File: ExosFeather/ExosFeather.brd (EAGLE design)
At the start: 50.8 x 22.9 mm, 12 parts, among them J2 TC_2050_IDC_TOP, J6 CONN_2X1_JST_PA, U1 MCP73831, U2 STM32L052KX

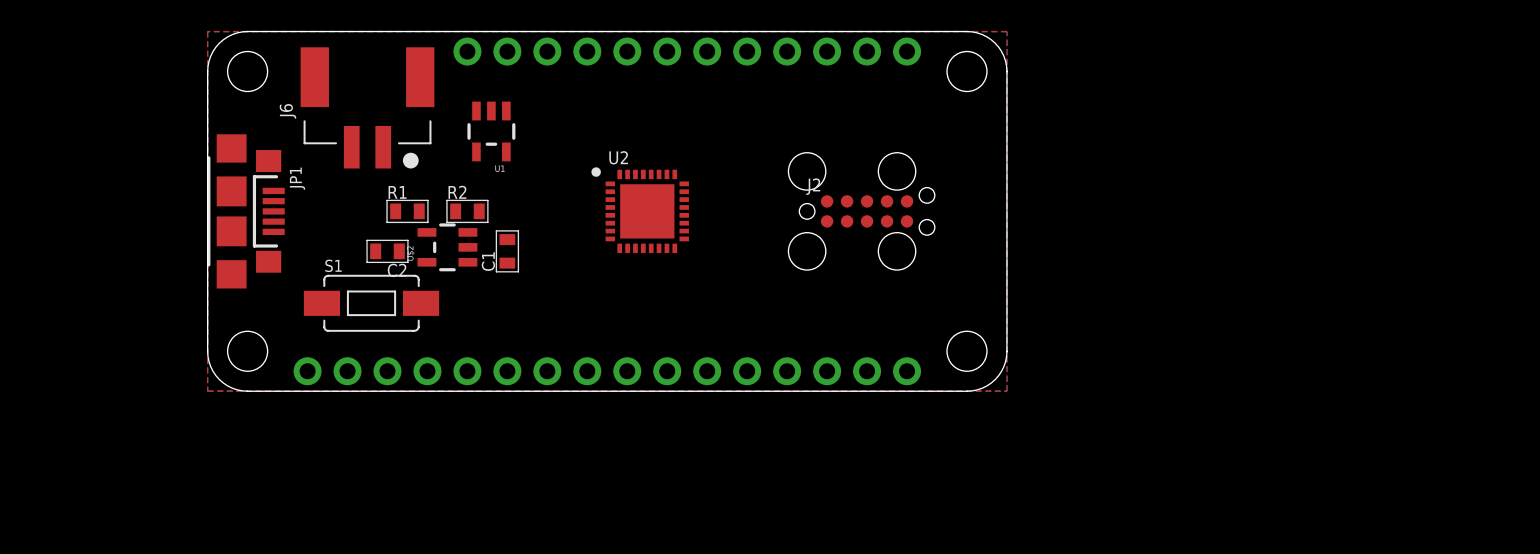
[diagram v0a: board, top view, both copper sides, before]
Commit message: exosfeather
updated the pinouts
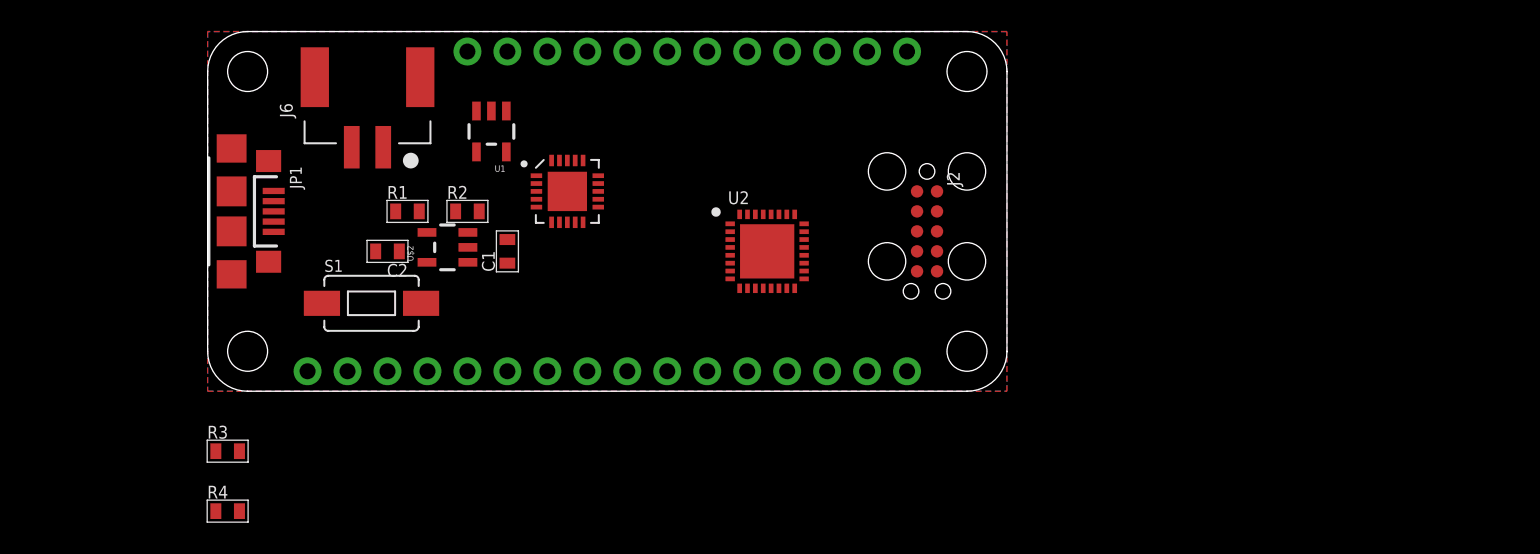
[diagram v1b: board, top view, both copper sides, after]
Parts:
- added R3, R4: (no value), stepOSP:0603
- added U$3: MCP73871, stepOSP:QFN_20_4X4
- moved U2 8.03 mm to (35.6, 8.89)
- moved J2 4.02 mm to (45.7, 10.2), turned to 270 degrees
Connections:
- new net CLK_IN: U$1.P$4, U2.6
- new net DAC: U$1.P$8, U2.10
- new net DE2: U$1.P$5, U2.7
- new net EVENT: U$1.P$23, U2.14
- new net MCO: U$1.P$24, U2.18
- new net MISO: U$1.P$16, U2.12
- new net MOSI: U$1.P$17, U2.13
- new net NRST: U$1.P$28, U2.4
- new net NSS: U$1.P$19, U2.25
- new net PB1: U$1.P$22, U2.15
- new net PB2: U$1.P$21, U2.16
- new net PB3: U$1.P$20, U2.26
- new net RX1: U$1.P$15, U2.20
- new net RX2: U$1.P$7, U2.9
- new net SCK: U$1.P$18, U2.11
- new net SCL: R3.P$1, U$1.P$11, U2.29
- new net SDA: R4.P$1, U$1.P$12, U2.30
- new net TIM22_CH1: U$1.P$9, U2.27
- new net TIM22_CH2: U$1.P$10, U2.28
- new net TX1: U$1.P$14, U2.19
- new net TX2: U$1.P$6, U2.8
- net +3V3: now also R3.P$2, R4.P$2
- net D+: now also U2.22
- net D-: now also U2.21
- net SW_CLK: now also U2.24
- net SW_DIO: now also U2.23
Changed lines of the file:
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@@
 <?xml version="1.0" encoding="utf-8"?>
 <!DOCTYPE eagle SYSTEM "eagle.dtd">
-<eagle version="7.7.0">
+<eagle version="7.3.0">
 <drawing>
 <settings>
@@
 <element name="R2" library="stepOSP" package="0603" value="" x="16.51" y="11.43"/>
 <element name="R1" library="stepOSP" package="0603" value="" x="12.7" y="11.43"/>
-<element name="U2" library="leaf" package="STM32_QFN_32_5X5" value="STM32L052KX" x="27.94" y="11.43"/>
-<element name="J2" library="leaf" package="TC_2050_IC_TOP" value="TC_2050_IDC_TOP" x="41.91" y="11.43"/>
+<element name="U2" library="leaf" package="STM32_QFN_32_5X5" value="STM32L052KX" x="35.56" y="8.89"/>
+<element name="J2" library="leaf" package="TC_2050_IC_TOP" value="TC_2050_IDC_TOP" x="45.72" y="10.16" rot="R270"/>
+<element name="R3" library="stepOSP" package="0603" value="" x="1.27" y="-3.81"/>
+<element name="R4" library="stepOSP" package="0603" value="" x="1.27" y="-7.62"/>
+<element name="U$3" library="stepOSP" package="QFN_20_4X4" value="MCP73871" x="22.86" y="12.7"/>
 </elements>
 <signals>
@@
 <contactref element="J2" pad="3"/>
 <contactref element="J2" pad="5"/>
-<wire x1="41.91" y1="10.795" x2="44.45" y2="10.795" width="0" layer="19" extent="1-1"/>
-<wire x1="44.45" y1="1.27" x2="44.45" y2="10.795" width="0" layer="19" extent="1-1"/>
-<wire x1="27.94" y1="11.43" x2="26.19" y2="13.78" width="0" layer="19" extent="1-1"/>
+<wire x1="45.085" y1="10.16" x2="45.085" y2="7.62" width="0" layer="19" extent="1-1"/>
+<wire x1="44.45" y1="1.27" x2="45.085" y2="7.62" width="0" layer="19" extent="1-1"/>
+<wire x1="35.56" y1="8.89" x2="33.81" y2="11.24" width="0" layer="19" extent="1-1"/>
 </signal>
 <signal name="N$4">
@@
 <signal name="D-">
 <contactref element="JP1" pad="D-"/>
+<contactref element="U2" pad="21"/>
+<wire x1="4.199" y1="12.08" x2="37.91" y2="9.14" width="0" layer="19" extent="1-1"/>
 </signal>
 <signal name="D+">
 <contactref element="JP1" pad="D+"/>
+<contactref element="U2" pad="22"/>
+<wire x1="4.199" y1="11.43" x2="37.91" y2="9.64" width="0" layer="19" extent="1-1"/>
 </signal>
 <signal name="N$8">
@@
 <contactref element="U2" pad="17"/>
 <contactref element="U2" pad="5"/>
-<wire x1="25.59" y1="11.18" x2="25.59" y2="13.18" width="0" layer="19" extent="1-1"/>
-<wire x1="30.29" y1="9.68" x2="25.59" y2="11.18" width="0" layer="19" extent="1-1"/>
-<wire x1="39.37" y1="10.795" x2="25.59" y2="11.18" width="0" layer="19" extent="1-1"/>
-<wire x1="8.89" y1="1.27" x2="39.37" y2="10.795" width="0" layer="19" extent="1-1"/>
+<contactref element="R4" pad="P$2"/>
+<contactref element="R3" pad="P$2"/>
+<wire x1="37.91" y1="7.14" x2="45.085" y2="12.7" width="0" layer="19" extent="1-1"/>
+<wire x1="33.21" y1="8.64" x2="37.91" y2="7.14" width="0" layer="19" extent="1-1"/>
+<wire x1="33.21" y1="10.64" x2="33.21" y2="8.64" width="0" layer="19" extent="1-1"/>
+<wire x1="8.89" y1="1.27" x2="33.21" y2="8.64" width="0" layer="19" extent="1-1"/>
+<wire x1="2.02" y1="-3.81" x2="8.89" y2="1.27" width="0" layer="19" extent="1-1"/>
+<wire x1="2.02" y1="-7.62" x2="2.02" y2="-3.81" width="0" layer="19" extent="1-1"/>
 </signal>
 <signal name="SW_DIO">
 <contactref element="J2" pad="2"/>
+<contactref element="U2" pad="23"/>
+<wire x1="37.91" y1="10.14" x2="45.085" y2="11.43" width="0" layer="19" extent="1-1"/>
 </signal>
 <signal name="N_RESET">
@@
 <signal name="SW_CLK">
 <contactref element="J2" pad="4"/>
+<contactref element="U2" pad="24"/>
+<wire x1="37.91" y1="10.64" x2="45.085" y2="8.89" width="0" layer="19" extent="1-1"/>
 </signal>
 <signal name="HRT_B">
@@
 <contactref element="J2" pad="9"/>
 </signal>
+<signal name="MOSI">
+<contactref element="U2" pad="13"/>
+<contactref element="U$1" pad="P$17"/>
+<wire x1="34.29" y1="1.27" x2="35.81" y2="6.54" width="0" layer="19" extent="1-1"/>
+</signal>
+<signal name="MISO">
+<contactref element="U2" pad="12"/>
+<contactref element="U$1" pad="P$16"/>
+<wire x1="35.31" y1="6.54" x2="36.83" y2="1.27" width="0" layer="19" extent="1-1"/>
+</signal>
+<signal name="SCK">
+<contactref element="U2" pad="11"/>
+<contactref element="U$1" pad="P$18"/>
+<wire x1="31.75" y1="1.27" x2="34.81" y2="6.54" width="0" layer="19" extent="1-1"/>
+</signal>
+<signal name="DAC">
+<contactref element="U2" pad="10"/>
+<contactref element="U$1" pad="P$8"/>
+<wire x1="34.31" y1="6.54" x2="34.29" y2="21.59" width="0" layer="19" extent="1-1"/>
+</signal>
+<signal name="DE2">
+<contactref element="U2" pad="7"/>
+<contactref element="U$1" pad="P$5"/>
+<wire x1="33.21" y1="7.64" x2="26.67" y2="21.59" width="0" layer="19" extent="1-1"/>
+</signal>
+<signal name="CLK_IN">
+<contactref element="U2" pad="6"/>
+<contactref element="U$1" pad="P$4"/>
+<wire x1="33.21" y1="8.14" x2="24.13" y2="21.59" width="0" layer="19" extent="1-1"/>
+</signal>
+<signal name="SCL">
+<contactref element="U$1" pad="P$11"/>
+<contactref element="U2" pad="29"/>
+<contactref element="R3" pad="P$1"/>
+<wire x1="35.31" y1="11.24" x2="41.91" y2="21.59" width="0" layer="19" extent="1-1"/>
+<wire x1="0.52" y1="-3.81" x2="35.31" y2="11.24" width="0" layer="19" extent="1-1"/>
+</signal>
+<signal name="SDA">
+<contactref element="U$1" pad="P$12"/>
+<contactref element="U2" pad="30"/>
+<contactref element="R4" pad="P$1"/>
+<wire x1="34.81" y1="11.24" x2="44.45" y2="21.59" width="0" layer="19" extent="1-1"/>
+<wire x1="0.52" y1="-7.62" x2="34.81" y2="11.24" width="0" layer="19" extent="1-1"/>
+</signal>
+<signal name="NRST">
+<contactref element="U$1" pad="P$28"/>
+<contactref element="U2" pad="4"/>
+<wire x1="6.35" y1="1.27" x2="33.21" y2="9.14" width="0" layer="19" extent="1-1"/>
+</signal>
+<signal name="PB3">
+<contactref element="U$1" pad="P$20"/>
+<contactref element="U2" pad="26"/>
+<wire x1="26.67" y1="1.27" x2="36.81" y2="11.24" width="0" layer="19" extent="1-1"/>
+</signal>
+<signal name="PB1">
+<contactref element="U$1" pad="P$22"/>
+<contactref element="U2" pad="15"/>
+<wire x1="21.59" y1="1.27" x2="36.81" y2="6.54" width="0" layer="19" extent="1-1"/>
+</signal>
+<signal name="TIM22_CH2">
+<contactref element="U2" pad="28"/>
+<contactref element="U$1" pad="P$10"/>
+<wire x1="35.81" y1="11.24" x2="39.37" y2="21.59" width="0" layer="19" extent="1-1"/>
+</signal>
+<signal name="TIM22_CH1">
+<contactref element="U2" pad="27"/>
+<contactref element="U$1" pad="P$9"/>
+<wire x1="36.31" y1="11.24" x2="36.83" y2="21.59" width="0" layer="19" extent="1-1"/>
+</signal>
+<signal name="RX2">
+<contactref element="U2" pad="9"/>
+<contactref element="U$1" pad="P$7"/>
+<wire x1="33.81" y1="6.54" x2="31.75" y2="21.59" width="0" layer="19" extent="1-1"/>
+</signal>
+<signal name="TX2">
+<contactref element="U2" pad="8"/>
+<contactref element="U$1" pad="P$6"/>
+<wire x1="33.21" y1="7.14" x2="29.21" y2="21.59" width="0" layer="19" extent="1-1"/>
+</signal>
+<signal name="RX1">
+<contactref element="U$1" pad="P$15"/>
+<contactref element="U2" pad="20"/>
+<wire x1="39.37" y1="1.27" x2="37.91" y2="8.64" width="0" layer="19" extent="1-1"/>
+</signal>
+<signal name="TX1">
+<contactref element="U$1" pad="P$14"/>
+<contactref element="U2" pad="19"/>
+<wire x1="37.91" y1="8.14" x2="41.91" y2="1.27" width="0" layer="19" extent="1-1"/>
+</signal>
+<signal name="MCO">
+<contactref element="U2" pad="18"/>
+<contactref element="U$1" pad="P$24"/>
+<wire x1="16.51" y1="1.27" x2="37.91" y2="7.64" width="0" layer="19" extent="1-1"/>
+</signal>
+<signal name="NSS">
+<contactref element="U2" pad="25"/>
+<contactref element="U$1" pad="P$19"/>
+<wire x1="29.21" y1="1.27" x2="37.31" y2="11.24" width="0" layer="19" extent="1-1"/>
+</signal>
+<signal name="EVENT">
+<contactref element="U2" pad="14"/>
+<contactref element="U$1" pad="P$23"/>
+<wire x1="19.05" y1="1.27" x2="36.31" y2="6.54" width="0" layer="19" extent="1-1"/>
+</signal>
+<signal name="PB2">
+<contactref element="U$1" pad="P$21"/>
+<contactref element="U2" pad="16"/>
+<wire x1="24.13" y1="1.27" x2="37.31" y2="6.54" width="0" layer="19" extent="1-1"/>
+</signal>
 </signals>

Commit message: exosfeather
added some new parts
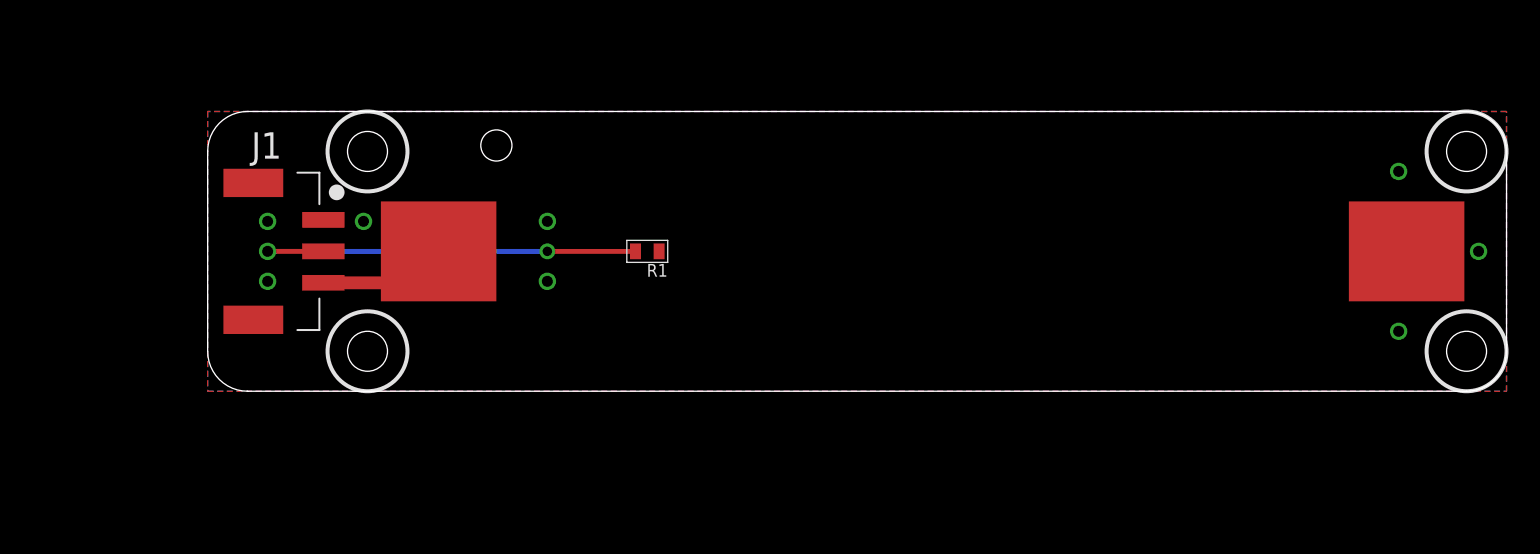
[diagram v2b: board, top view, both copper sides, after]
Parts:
- removed C1, C2, R2, R3, R4: (no value), stepOSP:0603
- removed J2: TC_2050_IDC_TOP, leaf:TC_2050_IC_TOP
- removed J6: CONN_2X1_JST_PA, leaf:CONN_2X1_JST_PA
- removed JP1: USB_MICROB_PLUG, stepOSP:USB-MICROB
- removed S1: SWITCH-MOMENTARY-2-SMD-1101NE, SparkFun-Electromechanical:TACTILE-SWITCH-1101NE
- removed U$1: FEATHER_PINOUT_FULL, stepOSP:FEATHER_PINOUT_FULL
- removed U$3: MCP73871, stepOSP:QFN_20_4X4
- removed U1: MCP73831, SparkFun-PowerIC:SOT23-5
- removed U2: STM32L052KX, leaf:STM32_QFN_32_5X5
- added J1: CONN_3X1_JST_PA, leaf:CONN_3X1_JST_PA
- U$2: value TPS709XX -> 14500_KEYSTONE_1024; device stepOSP:SOT23-5 -> stepOSP:14500_KEYSTONE_1024
- moved U$2 61.0 mm to (76.2, 8.89), turned to 180 degrees
- moved R1 15.5 mm to (27.9, 8.89), turned to 180 degrees
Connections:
- removed net +3V3: J2.1, R3.P$2, R4.P$2, U$1.P$27, U2.1, U2.17, U2.5
- removed net 3V3: C2.P$1, U$2.5
- removed net CLK_IN: U$1.P$4, U2.6
- removed net D+: JP1.D+, U2.22
- removed net D-: JP1.D-, U2.21
- removed net DAC: U$1.P$8, U2.10
- removed net DBG_RX: J2.9
- removed net DBG_TX: J2.8
- removed net DE2: U$1.P$5, U2.7
- removed net EN: U$1.P$2, U$2.3
- removed net EVENT: U$1.P$23, U2.14
- removed net HRT_B: J2.7
- removed net MCO: U$1.P$24, U2.18
- removed net MISO: U$1.P$16, U2.12
- removed net MOSI: U$1.P$17, U2.13
- removed net N$3: U1.4
- removed net N$4: J6.1
- removed net N$5: R1.P$1, R2.P$2, U1.5
- removed net N$6: U1.3
- removed net N$7: U1.2
- removed net NRST: U$1.P$28, U2.4
- removed net NSS: U$1.P$19, U2.25
- removed net N_RESET: J2.10
- removed net PB1: U$1.P$22, U2.15
- removed net PB2: U$1.P$21, U2.16
- removed net PB3: U$1.P$20, U2.26
- removed net RX1: U$1.P$15, U2.20
- removed net RX2: U$1.P$7, U2.9
- removed net SCK: U$1.P$18, U2.11
- removed net SCL: R3.P$1, U$1.P$11, U2.29
- removed net SDA: R4.P$1, U$1.P$12, U2.30
- removed net SWO: J2.6
- removed net SW_CLK: J2.4, U2.24
- removed net SW_DIO: J2.2, U2.23
- removed net TIM22_CH1: U$1.P$9, U2.27
- removed net TIM22_CH2: U$1.P$10, U2.28
- removed net TX1: U$1.P$14, U2.19
- removed net TX2: U$1.P$6, U2.8
- removed net VBAT: U$1.P$1
- removed net VBUS: U$1.P$3
- net GND: now also J1.1, R1.P$1, U$2.NEG; no longer J2.3, J2.5, J6.2, JP1.GND, U$1.P$13, U$1.P$25, U$2.2, U2.32, U2.GND
- net N$1: now also J1.2, R1.P$2; no longer C1.P$1, U$2.1
- net N$2: now also J1.3, U$2.POS; no longer JP1.VBUS
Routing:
- net N$1: track 0.00 -> 26.9 mm, vias 0 -> 2
- net N$2: track 0.00 -> 9.33 mm
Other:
- board size 50.8 x 22.9 mm -> 82.5 x 17.8 mm

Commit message: Revert "exosfeather"
This reverts commit d5dd059b457cfbbf08893ff69975569f2ea8e21c.
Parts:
- removed J1: CONN_3X1_JST_PA, leaf:CONN_3X1_JST_PA
- added C1, C2, R2, R3, R4: (no value), stepOSP:0603
- added J2: TC_2050_IDC_TOP, leaf:TC_2050_IC_TOP
- added J6: CONN_2X1_JST_PA, leaf:CONN_2X1_JST_PA
- added JP1: USB_MICROB_PLUG, stepOSP:USB-MICROB
- added S1: SWITCH-MOMENTARY-2-SMD-1101NE, SparkFun-Electromechanical:TACTILE-SWITCH-1101NE
- added U$1: FEATHER_PINOUT_FULL, stepOSP:FEATHER_PINOUT_FULL
- added U$3: MCP73871, stepOSP:QFN_20_4X4
- added U1: MCP73831, SparkFun-PowerIC:SOT23-5
- added U2: STM32L052KX, leaf:STM32_QFN_32_5X5
- U$2: value 14500_KEYSTONE_1024 -> TPS709XX; device stepOSP:14500_KEYSTONE_1024 -> stepOSP:SOT23-5
- moved U$2 61.0 mm to (15.2, 9.14), turned to 90 degrees
- moved R1 15.5 mm to (12.7, 11.4), turned to 0 degrees
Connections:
- new net +3V3: J2.1, R3.P$2, R4.P$2, U$1.P$27, U2.1, U2.17, U2.5
- new net 3V3: C2.P$1, U$2.5
- new net CLK_IN: U$1.P$4, U2.6
- new net D+: JP1.D+, U2.22
- new net D-: JP1.D-, U2.21
- new net DAC: U$1.P$8, U2.10
- new net DBG_RX: J2.9
- new net DBG_TX: J2.8
- new net DE2: U$1.P$5, U2.7
- new net EN: U$1.P$2, U$2.3
- new net EVENT: U$1.P$23, U2.14
- new net HRT_B: J2.7
- new net MCO: U$1.P$24, U2.18
- new net MISO: U$1.P$16, U2.12
- new net MOSI: U$1.P$17, U2.13
- new net N$3: U1.4
- new net N$4: J6.1
- new net N$5: R1.P$1, R2.P$2, U1.5
- new net N$6: U1.3
- new net N$7: U1.2
- new net NRST: U$1.P$28, U2.4
- new net NSS: U$1.P$19, U2.25
- new net N_RESET: J2.10
- new net PB1: U$1.P$22, U2.15
- new net PB2: U$1.P$21, U2.16
- new net PB3: U$1.P$20, U2.26
- new net RX1: U$1.P$15, U2.20
- new net RX2: U$1.P$7, U2.9
- new net SCK: U$1.P$18, U2.11
- new net SCL: R3.P$1, U$1.P$11, U2.29
- new net SDA: R4.P$1, U$1.P$12, U2.30
- new net SWO: J2.6
- new net SW_CLK: J2.4, U2.24
- new net SW_DIO: J2.2, U2.23
- new net TIM22_CH1: U$1.P$9, U2.27
- new net TIM22_CH2: U$1.P$10, U2.28
- new net TX1: U$1.P$14, U2.19
- new net TX2: U$1.P$6, U2.8
- new net VBAT: U$1.P$1
- new net VBUS: U$1.P$3
- net GND: now also J2.3, J2.5, J6.2, JP1.GND, U$1.P$13, U$1.P$25, U$2.2, U2.32, U2.GND; no longer J1.1, R1.P$1, U$2.NEG
- net N$1: now also C1.P$1, U$2.1; no longer J1.2, R1.P$2
- net N$2: now also JP1.VBUS; no longer J1.3, U$2.POS
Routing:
- net N$1: track 26.9 -> 0.00 mm, vias 2 -> 0
- net N$2: track 9.33 -> 0.00 mm
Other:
- board size 82.5 x 17.8 mm -> 50.8 x 22.9 mm

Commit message: exofeather update
latest and greates exofeather
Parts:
- removed U$3: MCP73871, stepOSP:QFN_20_4X4
- added C3, C4, R5: (no value), stepOSP:0603
- added D1: 0603_LED, stepOSP:0603_LED
- added J1: JST_PH_2_PTH, stepOSP:JST_PH_PTH_2
- added U$17: TC_2050_IDC_TOP, leaf:TC_2050_IC_TOP
- added U3: TI_CHGR_BQ21040, leaf:SOT-23-6_TI
- U1: value MCP73831 -> TVS_USB_TPD4S012; device SparkFun-PowerIC:SOT23-5 -> leaf:USB_TVS_TPD4S012
- moved R4 50.4 mm to (44.5, 18.4), turned to 270 degrees
- moved R3 46.2 mm to (41.8, 18.4), turned to 270 degrees
- moved U1 12.7 mm to (6.62, 11.0), turned to 0 degrees
- moved C2 11.4 mm to (22.8, 9.25)
- moved U$2 8.07 mm to (22.6, 12.4), turned to 180 degrees
- moved C1 7.40 mm to (22.8, 15.3), turned to 180 degrees
- moved R1 3.34 mm to (9.36, 11.5)
- moved U2 3.17 mm to (33.0, 10.7), turned to 270 degrees
- moved R2 2.44 mm to (18.9, 11.4), turned to 90 degrees
- moved J2 1.28 mm to (45.5, 11.4), turned to 0 degrees
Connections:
- removed net 3V3: C2.P$1, U$2.5
- removed net DBG_RX: J2.9
- removed net DBG_TX: J2.8
- removed net HRT_B: J2.7
- removed net N$1: C1.P$1, U$2.1
- removed net N$2: JP1.VBUS
- removed net N$4: J6.1
- net +3V3: now also C2.P$1, U$2.5
- net D+: now also U1.1
- net D-: now also U1.2
- net GND: now also C1.P$2, C2.P$2, C3.P$2, C4.P$2, J6.1, R1.P$1, R2.P$2, U1.4, U3.5; no longer J6.2
- net MCO: now also J2.7
- net N$3: now also J1.P$2, R2.P$1, U3.1; no longer U1.4
- net N$5: now also R1.P$2, U3.4; no longer R1.P$1, R2.P$2, U1.5
- net N$6: now also D1.P$2, U3.3; no longer U1.3
- net N$7: now also D1.P$1, R5.P$1; no longer U1.2
- net RX1: now also J2.9
- net TX1: now also J2.8
- net VBAT: now also C1.P$1, C4.P$1, J6.2, R5.P$2, U$2.1, U3.2
- net VBUS: now also C3.P$1, JP1.VBUS, U1.6, U3.6
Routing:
- net VBAT: track 0.00 -> 34.3 mm, vias 0 -> 2
- net VBUS: track 0.00 -> 33.6 mm, vias 0 -> 1
- net D-: track 0.00 -> 33.5 mm, vias 0 -> 3
- net D+: track 0.00 -> 27.4 mm, vias 0 -> 2
- net EVENT: track 0.00 -> 15.2 mm
- net CLK_IN: track 0.00 -> 14.9 mm
- net TIM22_CH2: track 0.00 -> 14.6 mm
- net PB1: track 0.00 -> 12.6 mm
- net DE2: track 0.00 -> 12.2 mm, vias 0 -> 1
- net RX2: track 0.00 -> 11.3 mm, vias 0 -> 1
- net TX2: track 0.00 -> 11.1 mm, vias 0 -> 1
- net PB2: track 0.00 -> 10.5 mm
- net EN: track 0.00 -> 9.03 mm
- net +3V3: track 0.00 -> 7.60 mm
- net SCK: track 0.00 -> 7.33 mm
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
